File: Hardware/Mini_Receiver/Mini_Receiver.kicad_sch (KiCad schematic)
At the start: 13 parts, among them J1 Conn_01x10_Male, J2 Conn_01x10_Male, J3 Conn_01x10_Male, SW1 KEY, U1 STC8H1K28_LQFP32, U2 XC6206PxxxMR, U3 RF24_SMD

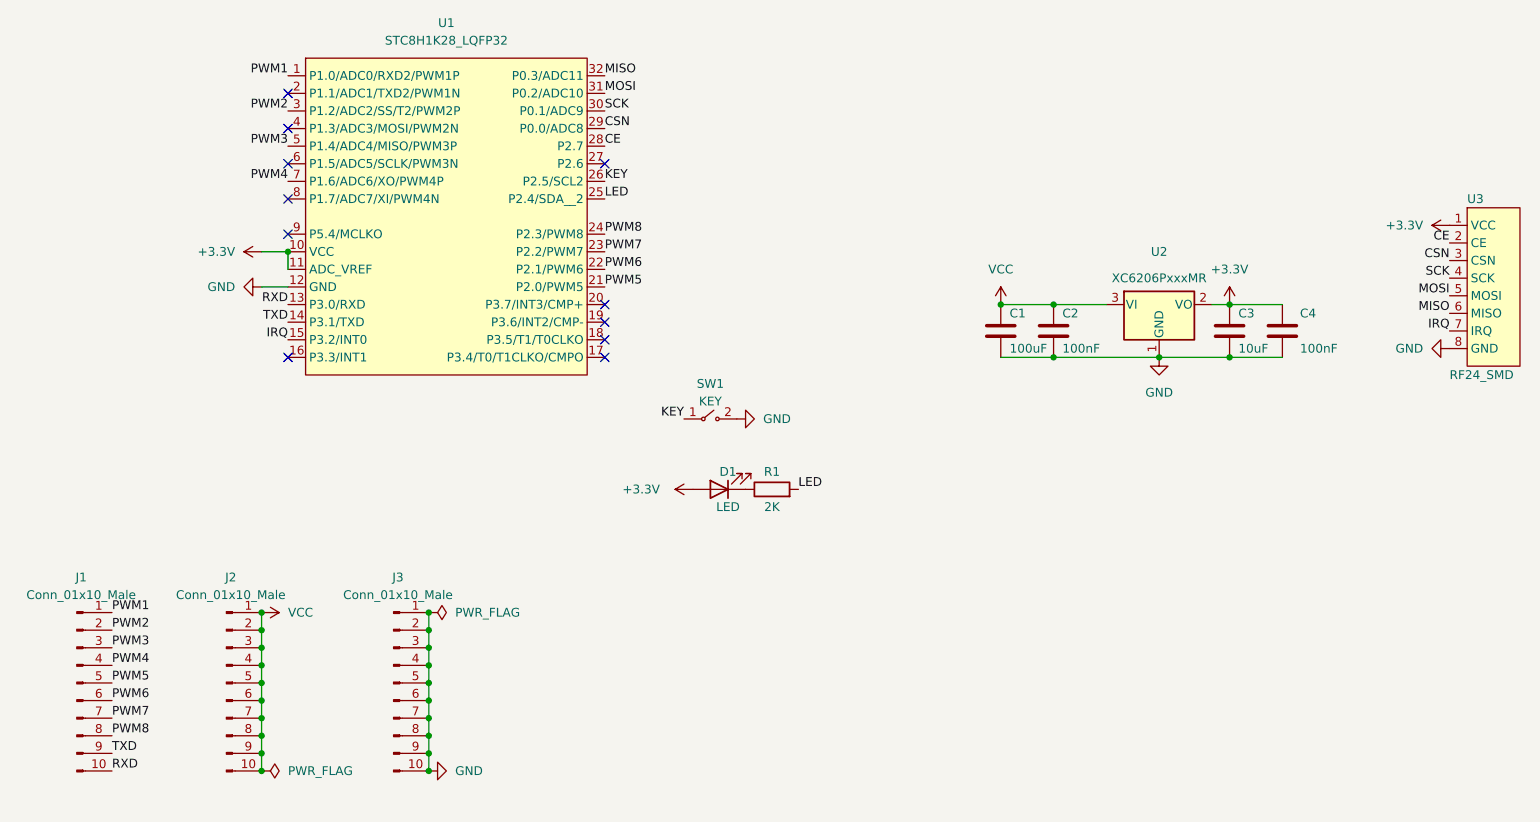
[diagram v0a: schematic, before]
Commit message: 完成12通道接收机PCB初板设计并发送打样，等待验证
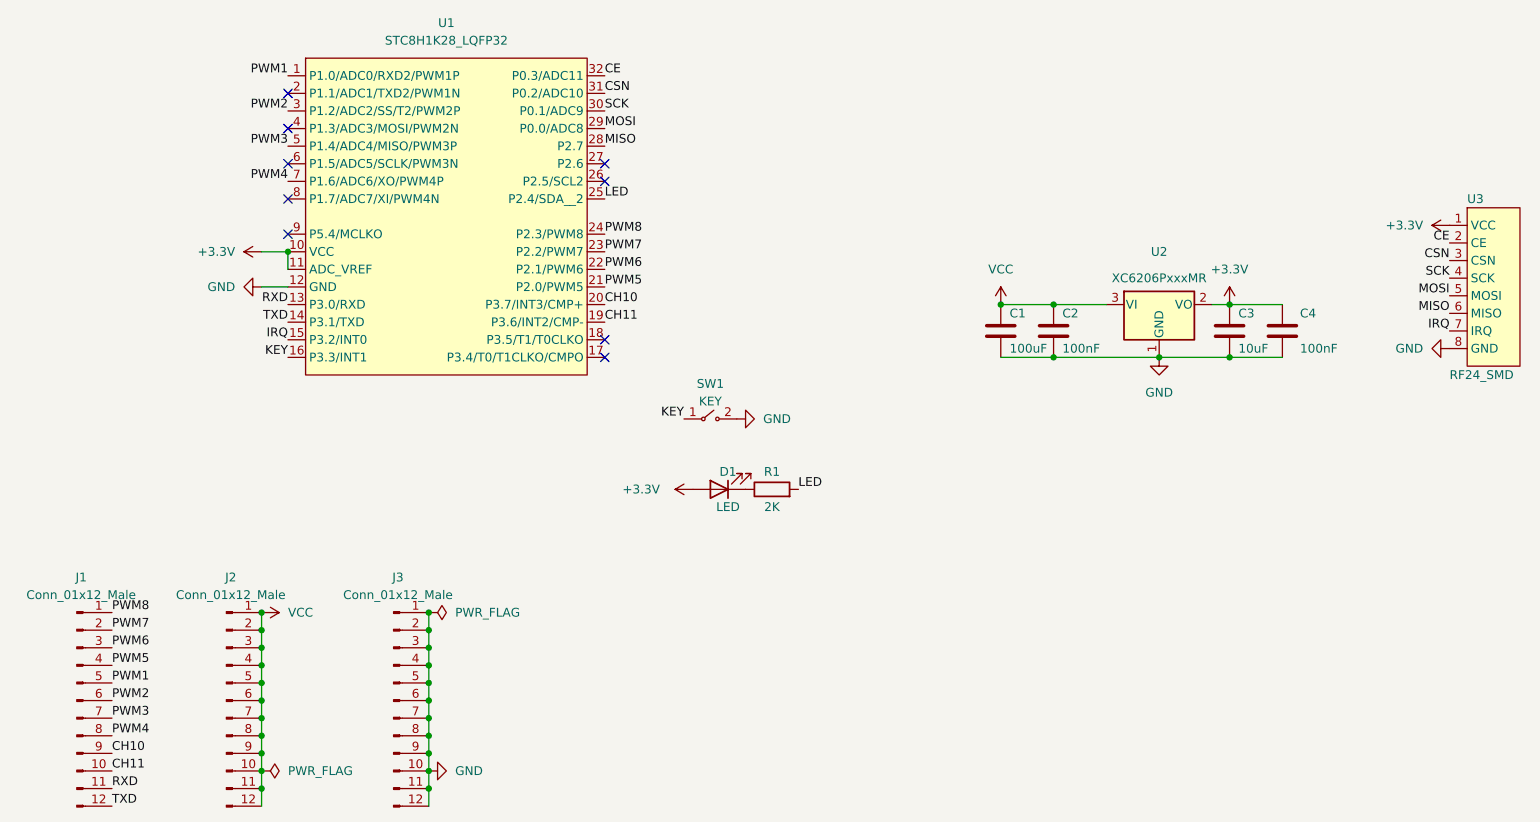
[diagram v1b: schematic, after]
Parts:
- removed J1, J2, J3: Conn_01x10_Male, Connector_PinHeader_2.54mm:PinHeader_1x10_P2.54mm_Vertical, symbol Connector:Conn_01x10_Male
- added J1, J2, J3: Conn_01x12_Male, Connector_PinHeader_2.54mm:PinHeader_1x12_P2.54mm_Vertical, symbol Connector:Conn_01x12_Male
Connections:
- net CE: now also U1.32 (P0.3/ADC11); no longer U1.28 (P2.7)
- net CSN: now also U1.31 (P0.2/ADC10); no longer U1.29 (P0.0/ADC8)
- net GND: now also J3.1 (Pin_1), J3.10 (Pin_10), J3.11 (Pin_11), J3.12 (Pin_12), J3.2 (Pin_2), J3.3 (Pin_3), J3.4 (Pin_4), J3.5 (Pin_5), J3.6 (Pin_6), J3.7 (Pin_7), J3.8 (Pin_8), J3.9 (Pin_9)
- net KEY: now also U1.16 (P3.3/INT1); no longer U1.26 (P2.5/SCL2)
- net MISO: now also U1.28 (P2.7); no longer U1.32 (P0.3/ADC11)
- net MOSI: now also U1.29 (P0.0/ADC8); no longer U1.31 (P0.2/ADC10)
- net PWM1: now also J1.5 (Pin_5)
- net PWM2: now also J1.6 (Pin_6)
- net PWM3: now also J1.7 (Pin_7)
- net PWM4: now also J1.8 (Pin_8)
- net PWM5: now also J1.4 (Pin_4)
- net PWM6: now also J1.3 (Pin_3)
- net PWM7: now also J1.2 (Pin_2)
- net PWM8: now also J1.1 (Pin_1)
- net RXD: now also J1.11 (Pin_11)
- net TXD: now also J1.12 (Pin_12)
- net VCC: now also J2.1 (Pin_1), J2.10 (Pin_10), J2.11 (Pin_11), J2.12 (Pin_12), J2.2 (Pin_2), J2.3 (Pin_3), J2.4 (Pin_4), J2.5 (Pin_5), J2.6 (Pin_6), J2.7 (Pin_7), J2.8 (Pin_8), J2.9 (Pin_9)
- net CH11: now reaches U1.19 (P3.6/INT2/CMP-)
- net CH11: now also J1.10 (Pin_10)
- net CH10: now reaches U1.20 (P3.7/INT3/CMP+)
- net CH10: now also J1.9 (Pin_9)
- no-connect marks 11 -> 9
